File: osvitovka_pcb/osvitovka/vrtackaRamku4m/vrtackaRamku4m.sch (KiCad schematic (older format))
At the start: 17 parts, among them J1 Screw_Terminal_01x01, J2 Screw_Terminal_01x01, J3 M+, J4 M-, K1 RSM822, Q1 BC817, U1 LM78M05_TO220

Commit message: Nový PCB.
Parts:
- added D1, D2: D, Diode_SMD:D_1206_3216Metric, symbol Device:D
- added H1, H2: MountingHole, MountingHole:MountingHole_3.2mm_M3_ISO14580, symbol Mechanical:MountingHole
- R1, R2, R3, R4: footprint Resistor_SMD:R_1206_3216Metric_Pad1.42x1.75mm_HandSolder -> Resistor_SMD:R_0805_2012Metric
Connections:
- net +12V: now also D1.1 (K)
- net +5V: now also R4.2
- net GND: now also D2.2 (A)
- net at J3.1 (Pin_1), K1.14, K1.24: now also D2.1 (K)
- net at K1.A1, Q1.3 (C): now also D1.2 (A)
- net Led_green: no longer names the net of A1.13 (D10)
- net Led_green: no longer R4.2
- no-connect marks 25 -> 26
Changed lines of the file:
@@
 F 0 "R1" V 5143 2600 50  0000 C CNN
 F 1 "4k7" V 5234 2600 50  0000 C CNN
-F 2 "Resistor_SMD:R_1206_3216Metric_Pad1.42x1.75mm_HandSolder" V 5280 2600 50  0001 C CNN
+F 2 "Resistor_SMD:R_0805_2012Metric" V 5280 2600 50  0001 C CNN
 F 3 "~" H 5350 2600 50  0001 C CNN
 	1    5350 2600
@@
 F 0 "R3" V 1543 4600 50  0000 C CNN
 F 1 "470" V 1634 4600 50  0000 C CNN
-F 2 "Resistor_SMD:R_1206_3216Metric_Pad1.42x1.75mm_HandSolder" V 1680 4600 50  0001 C CNN
+F 2 "Resistor_SMD:R_0805_2012Metric" V 1680 4600 50  0001 C CNN
 F 3 "~" H 1750 4600 50  0001 C CNN
 	1    1750 4600
@@
 Text GLabel 1400 4600 0    50   Input ~ 0
 Led_yellow
-Text GLabel 1400 5050 0    50   Input ~ 0
-Led_green
 $Comp
 L Device:R R4
@@
 F 0 "R4" V 1543 5050 50  0000 C CNN
 F 1 "470" V 1634 5050 50  0000 C CNN
-F 2 "Resistor_SMD:R_1206_3216Metric_Pad1.42x1.75mm_HandSolder" V 1680 5050 50  0001 C CNN
+F 2 "Resistor_SMD:R_0805_2012Metric" V 1680 5050 50  0001 C CNN
 F 3 "~" H 1750 5050 50  0001 C CNN
 	1    1750 5050
@@
 Text GLabel 8500 3350 0    50   Input ~ 0
 Led_yellow
-Text GLabel 8500 3450 0    50   Input ~ 0
-Led_green
 Wire Wire Line
 	1250 3600 1400 3600
@@
 NoConn ~ 10050 2550
 NoConn ~ 10050 2450
-Wire Wire Line
-	8500 3450 9050 3450
 NoConn ~ 9050 2450
 NoConn ~ 9050 2650
@@
 	7000 2850 7000 3050
 Wire Wire Line
-	6100 2200 6100 2400
+	6100 2200 6100 2300
 $Comp
 L power:+12V #PWR03
@@
 $EndComp
 Wire Wire Line
-	6100 1450 6100 1600
+	6100 1450 6100 1550
 $Comp
 L power:GND #PWR011
@@
 F 0 "R2" V 5443 2800 50  0000 C CNN
 F 1 "10k" V 5534 2800 50  0000 C CNN
-F 2 "Resistor_SMD:R_1206_3216Metric_Pad1.42x1.75mm_HandSolder" V 5580 2800 50  0001 C CNN
+F 2 "Resistor_SMD:R_0805_2012Metric" V 5580 2800 50  0001 C CNN
 F 3 "~" H 5650 2800 50  0001 C CNN
 	1    5650 2800
@@
 NoConn ~ 6400 2200
 NoConn ~ 6800 2200
+$Comp
+L Mechanical:MountingHole H1
+U 1 1 5FD664D9
+P 1000 5500
+F 0 "H1" H 1100 5546 50  0000 L CNN
+F 1 "MountingHole" H 1100 5455 50  0000 L CNN
+F 2 "MountingHole:MountingHole_3.2mm_M3_ISO14580" H 1000 5500 50  0001 C CNN
+F 3 "~" H 1000 5500 50  0001 C CNN
+	1    1000 5500
+	1    0    0    -1
+$EndComp
+$Comp
+L Mechanical:MountingHole H2
+U 1 1 5FD66F45
+P 1000 5700
+F 0 "H2" H 1100 5746 50  0000 L CNN
+F 1 "MountingHole" H 1100 5655 50  0000 L CNN
+F 2 "MountingHole:MountingHole_3.2mm_M3_ISO14580" H 1000 5700 50  0001 C CNN
+F 3 "~" H 1000 5700 50  0001 C CNN
+	1    1000 5700
+	1    0    0    -1
+$EndComp
+$Comp
+L Device:D D2
+U 1 1 5FD94B8B
+P 7000 2650
+F 0 "D2" V 6954 2729 50  0000 L CNN
+F 1 "D" V 7045 2729 50  0000 L CNN
+F 2 "Diode_SMD:D_1206_3216Metric" H 7000 2650 50  0001 C CNN
+F 3 "~" H 7000 2650 50  0001 C CNN
+	1    7000 2650
+	0    1    1    0
+$EndComp
+$Comp
+L Device:D D1
+U 1 1 5FD95C5D
+P 5700 1900
+F 0 "D1" H 5700 2116 50  0000 C CNN
+F 1 "D" H 5700 2025 50  0000 C CNN
+F 2 "Diode_SMD:D_1206_3216Metric" H 5700 1900 50  0001 C CNN
+F 3 "~" H 5700 1900 50  0001 C CNN
+	1    5700 1900
+	0    1    1    0
+$EndComp
+Wire Wire Line
+	5700 1750 5700 1550
+Wire Wire Line
+	5700 1550 6100 1550
+Connection ~ 6100 1550
+Wire Wire Line
+	6100 1550 6100 1600
+Wire Wire Line
+	5700 2050 5700 2300
+Wire Wire Line
+	5700 2300 6100 2300
+Connection ~ 6100 2300
+Wire Wire Line
+	6100 2300 6100 2400
+Wire Wire Line
+	7000 2800 7000 2850
+Connection ~ 7000 2850
+Wire Wire Line
+	7000 2500 7000 2450
+$Comp
+L power:+5V #PWR?
+U 1 1 5FDA6872
+P 1400 5050
+F 0 "#PWR?" H 1400 4900 50  0001 C CNN
+F 1 "+5V" V 1415 5178 50  0000 L CNN
+F 2 "" H 1400 5050 50  0001 C CNN
+F 3 "" H 1400 5050 50  0001 C CNN
+	1    1400 5050
+	0    -1   -1   0
+$EndComp
+NoConn ~ 9050 3450
 $EndSCHEMATC

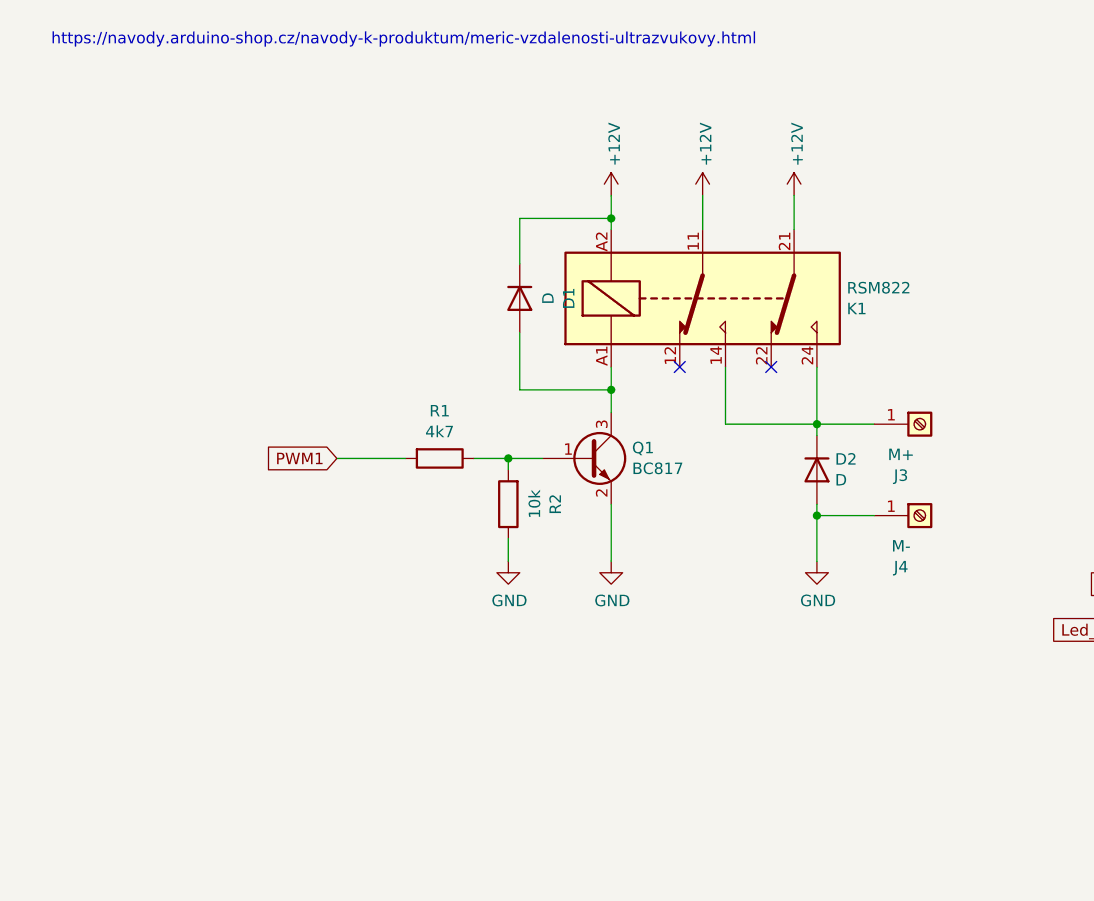
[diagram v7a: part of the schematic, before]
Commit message: Měl jsem špatný pouzdro na relátku. Opraveno.
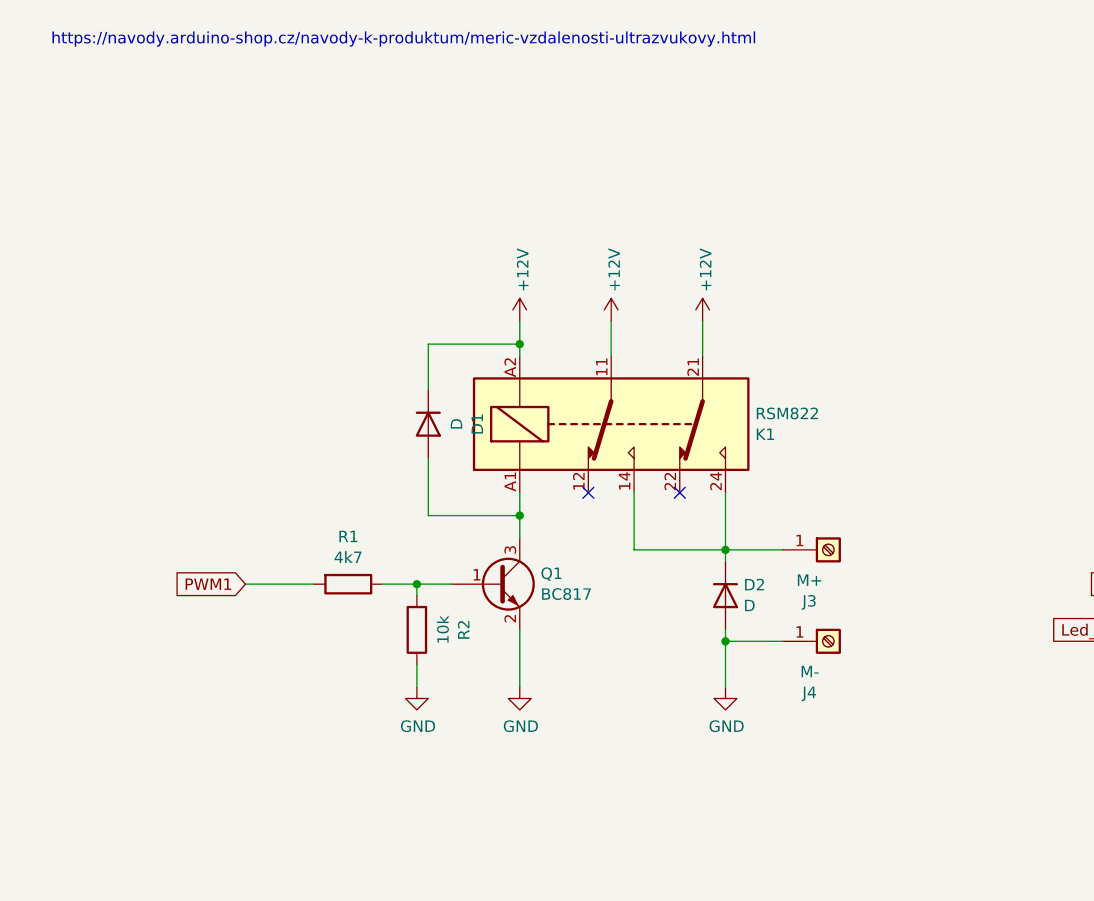
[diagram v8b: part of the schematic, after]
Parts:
- K1: footprint Relay_THT:Relay_DPDT_Finder_40.52 -> Relay_THT:Relay_DPDT_Finder_30.22
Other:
- moved on the sheet: D1, D2, J3, J4, K1, Q1, R1, R2
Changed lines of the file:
@@
 L power:GND #PWR010
 U 1 1 5FCC4DA2
-P 5650 3050
-F 0 "#PWR010" H 5650 2800 50  0001 C CNN
-F 1 "GND" H 5655 2877 50  0000 C CNN
-F 2 "" H 5650 3050 50  0001 C CNN
-F 3 "" H 5650 3050 50  0001 C CNN
-	1    5650 3050
+P 5250 3600
+F 0 "#PWR010" H 5250 3350 50  0001 C CNN
+F 1 "GND" H 5255 3427 50  0000 C CNN
+F 2 "" H 5250 3600 50  0001 C CNN
+F 3 "" H 5250 3600 50  0001 C CNN
+	1    5250 3600
 	1    0    0    -1
 $EndComp
@@
 L Device:R R1
 U 1 1 5FCC5E82
-P 5350 2600
-F 0 "R1" V 5143 2600 50  0000 C CNN
-F 1 "4k7" V 5234 2600 50  0000 C CNN
-F 2 "Resistor_SMD:R_0805_2012Metric" V 5280 2600 50  0001 C CNN
-F 3 "~" H 5350 2600 50  0001 C CNN
-	1    5350 2600
-	0    1    1    0
-$EndComp
-Text GLabel 4900 2600 0    50   Input ~ 0
+P 4950 3150
+F 0 "R1" V 4743 3150 50  0000 C CNN
+F 1 "4k7" V 4834 3150 50  0000 C CNN
+F 2 "Resistor_SMD:R_0805_2012Metric" V 4880 3150 50  0001 C CNN
+F 3 "~" H 4950 3150 50  0001 C CNN
+	1    4950 3150
+	0    1    1    0
+$EndComp
+Text GLabel 4500 3150 0    50   Input ~ 0
 PWM1
 Wire Wire Line
-	4900 2600 5200 2600
+	4500 3150 4800 3150
 Text GLabel 8500 3150 0    50   Input ~ 0
 PWM1
@@
 L Connector:Screw_Terminal_01x01 J3
 U 1 1 5FD0CD16
-P 7450 2450
-F 0 "J3" H 7368 2225 50  0000 C CNN
-F 1 "M+" H 7368 2316 50  0000 C CNN
-F 2 "TestPoint:TestPoint_Loop_D3.80mm_Drill2.5mm" H 7450 2450 50  0001 C CNN
-F 3 "~" H 7450 2450 50  0001 C CNN
-	1    7450 2450
+P 7050 3000
+F 0 "J3" H 6968 2775 50  0000 C CNN
+F 1 "M+" H 6968 2866 50  0000 C CNN
+F 2 "TestPoint:TestPoint_Loop_D3.80mm_Drill2.5mm" H 7050 3000 50  0001 C CNN
+F 3 "~" H 7050 3000 50  0001 C CNN
+	1    7050 3000
 	1    0    0    -1
 $EndComp
@@
 L Connector:Screw_Terminal_01x01 J4
 U 1 1 5FD0DE67
-P 7450 2850
-F 0 "J4" H 7368 2625 50  0000 C CNN
-F 1 "M-" H 7368 2716 50  0000 C CNN
-F 2 "TestPoint:TestPoint_Loop_D3.80mm_Drill2.5mm" H 7450 2850 50  0001 C CNN
-F 3 "~" H 7450 2850 50  0001 C CNN
-	1    7450 2850
+P 7050 3400
+F 0 "J4" H 6968 3175 50  0000 C CNN
+F 1 "M-" H 6968 3266 50  0000 C CNN
+F 2 "TestPoint:TestPoint_Loop_D3.80mm_Drill2.5mm" H 7050 3400 50  0001 C CNN
+F 3 "~" H 7050 3400 50  0001 C CNN
+	1    7050 3400
 	1    0    0    -1
 $EndComp
@@
 L Transistor_BJT:BC817 Q1
 U 1 1 5FD6B85F
-P 6000 2600
-F 0 "Q1" H 6191 2646 50  0000 L CNN
-F 1 "BC817" H 6191 2555 50  0000 L CNN
-F 2 "Package_TO_SOT_SMD:SOT-23" H 6200 2525 50  0001 L CIN
-F 3 "http://www.fairchildsemi.com/ds/BC/BC817.pdf" H 6000 2600 50  0001 L CNN
-	1    6000 2600
+P 5600 3150
+F 0 "Q1" H 5791 3196 50  0000 L CNN
+F 1 "BC817" H 5791 3105 50  0000 L CNN
+F 2 "Package_TO_SOT_SMD:SOT-23" H 5800 3075 50  0001 L CIN
+F 3 "http://www.fairchildsemi.com/ds/BC/BC817.pdf" H 5600 3150 50  0001 L CNN
+	1    5600 3150
 	1    0    0    -1
 $EndComp
@@
 L Relay:RSM822 K1
 U 1 1 5FD72A40
-P 6500 1900
-F 0 "K1" H 7130 1946 50  0000 L CNN
-F 1 "RSM822" H 7130 1855 50  0000 L CNN
-F 2 "Relay_THT:Relay_DPDT_Finder_40.52" H 7850 1870 50  0001 C CNN
-F 3 "http://www.relpol.pl/en/content/download/14975/202519/file/e_RSM822.pdf" H 6500 1900 50  0001 C CNN
-	1    6500 1900
+P 6100 2450
+F 0 "K1" H 6730 2496 50  0000 L CNN
+F 1 "RSM822" H 6730 2405 50  0000 L CNN
+F 2 "Relay_THT:Relay_DPDT_Finder_30.22" H 7450 2420 50  0001 C CNN
+F 3 "http://www.relpol.pl/en/content/download/14975/202519/file/e_RSM822.pdf" H 6100 2450 50  0001 C CNN
+	1    6100 2450
 	1    0    0    1
 $EndComp
@@
 L power:+12V #PWR04
 U 1 1 5FD831EA
-P 6500 1450
-F 0 "#PWR04" H 6500 1300 50  0001 C CNN
-F 1 "+12V" V 6515 1578 50  0000 L CNN
-F 2 "" H 6500 1450 50  0001 C CNN
-F 3 "" H 6500 1450 50  0001 C CNN
-	1    6500 1450
+P 6100 2000
+F 0 "#PWR04" H 6100 1850 50  0001 C CNN
+F 1 "+12V" V 6115 2128 50  0000 L CNN
+F 2 "" H 6100 2000 50  0001 C CNN
+F 3 "" H 6100 2000 50  0001 C CNN
+	1    6100 2000
 	1    0    0    -1
 $EndComp
@@
 L power:+12V #PWR05
 U 1 1 5FD83A62
-P 6900 1450
-F 0 "#PWR05" H 6900 1300 50  0001 C CNN
-F 1 "+12V" V 6915 1578 50  0000 L CNN
-F 2 "" H 6900 1450 50  0001 C CNN
-F 3 "" H 6900 1450 50  0001 C CNN
-	1    6900 1450
-	1    0    0    -1
-$EndComp
-Wire Wire Line
-	6500 1450 6500 1600
-Wire Wire Line
-	6900 1450 6900 1600
-Wire Wire Line
-	7250 2450 7000 2450
-Wire Wire Line
-	6600 2450 6600 2200
-Wire Wire Line
-	7000 2200 7000 2450
-Connection ~ 7000 2450
-Wire Wire Line
-	7000 2450 6600 2450
+P 6500 2000
+F 0 "#PWR05" H 6500 1850 50  0001 C CNN
+F 1 "+12V" V 6515 2128 50  0000 L CNN
+F 2 "" H 6500 2000 50  0001 C CNN
+F 3 "" H 6500 2000 50  0001 C CNN
+	1    6500 2000
+	1    0    0    -1
+$EndComp
+Wire Wire Line
+	6100 2000 6100 2150
+Wire Wire Line
+	6500 2000 6500 2150
+Wire Wire Line
+	6850 3000 6600 3000
+Wire Wire Line
+	6200 3000 6200 2750
+Wire Wire Line
+	6600 2750 6600 3000
+Connection ~ 6600 3000
+Wire Wire Line
+	6600 3000 6200 3000
 $Comp
 L power:GND #PWR012
 U 1 1 5FD86ED6
-P 7000 3050
-F 0 "#PWR012" H 7000 2800 50  0001 C CNN
-F 1 "GND" H 7005 2877 50  0000 C CNN
-F 2 "" H 7000 3050 50  0001 C CNN
-F 3 "" H 7000 3050 50  0001 C CNN
-	1    7000 3050
-	1    0    0    -1
-$EndComp
-Wire Wire Line
-	7250 2850 7000 2850
-Wire Wire Line
-	7000 2850 7000 3050
-Wire Wire Line
-	6100 2200 6100 2300
+P 6600 3600
+F 0 "#PWR012" H 6600 3350 50  0001 C CNN
+F 1 "GND" H 6605 3427 50  0000 C CNN
+F 2 "" H 6600 3600 50  0001 C CNN
+F 3 "" H 6600 3600 50  0001 C CNN
+	1    6600 3600
+	1    0    0    -1
+$EndComp
+Wire Wire Line
+	6850 3400 6600 3400
+Wire Wire Line
+	6600 3400 6600 3600
+Wire Wire Line
+	5700 2750 5700 2850
 $Comp
 L power:+12V #PWR03
 U 1 1 5FD8968E
-P 6100 1450
-F 0 "#PWR03" H 6100 1300 50  0001 C CNN
-F 1 "+12V" V 6115 1578 50  0000 L CNN
-F 2 "" H 6100 1450 50  0001 C CNN
-F 3 "" H 6100 1450 50  0001 C CNN
-	1    6100 1450
-	1    0    0    -1
-$EndComp
-Wire Wire Line
-	6100 1450 6100 1550
+P 5700 2000
+F 0 "#PWR03" H 5700 1850 50  0001 C CNN
+F 1 "+12V" V 5715 2128 50  0000 L CNN
+F 2 "" H 5700 2000 50  0001 C CNN
+F 3 "" H 5700 2000 50  0001 C CNN
+	1    5700 2000
+	1    0    0    -1
+$EndComp
+Wire Wire Line
+	5700 2000 5700 2100
 $Comp
 L power:GND #PWR011
 U 1 1 5FD8A380
-P 6100 3050
-F 0 "#PWR011" H 6100 2800 50  0001 C CNN
-F 1 "GND" H 6105 2877 50  0000 C CNN
-F 2 "" H 6100 3050 50  0001 C CNN
-F 3 "" H 6100 3050 50  0001 C CNN
-	1    6100 3050
-	1    0    0    -1
-$EndComp
-Wire Wire Line
-	6100 2800 6100 3050
+P 5700 3600
+F 0 "#PWR011" H 5700 3350 50  0001 C CNN
+F 1 "GND" H 5705 3427 50  0000 C CNN
+F 2 "" H 5700 3600 50  0001 C CNN
+F 3 "" H 5700 3600 50  0001 C CNN
+	1    5700 3600
+	1    0    0    -1
+$EndComp
+Wire Wire Line
+	5700 3350 5700 3600
 $Comp
 L Device:R R2
 U 1 1 5FD8CC29
-P 5650 2800
-F 0 "R2" V 5443 2800 50  0000 C CNN
-F 1 "10k" V 5534 2800 50  0000 C CNN
-F 2 "Resistor_SMD:R_0805_2012Metric" V 5580 2800 50  0001 C CNN
-F 3 "~" H 5650 2800 50  0001 C CNN
-	1    5650 2800
+P 5250 3350
+F 0 "R2" V 5043 3350 50  0000 C CNN
+F 1 "10k" V 5134 3350 50  0000 C CNN
+F 2 "Resistor_SMD:R_0805_2012Metric" V 5180 3350 50  0001 C CNN
+F 3 "~" H 5250 3350 50  0001 C CNN
+	1    5250 3350
 	-1   0    0    1
 $EndComp
 Wire Wire Line
-	5500 2600 5650 2600
-Wire Wire Line
-	5650 2650 5650 2600
-Connection ~ 5650 2600
-Wire Wire Line
-	5650 2600 5800 2600
-Wire Wire Line
-	5650 2950 5650 3050
-NoConn ~ 6400 2200
-NoConn ~ 6800 2200
+	5100 3150 5250 3150
+Wire Wire Line
+	5250 3200 5250 3150
+Connection ~ 5250 3150
+Wire Wire Line
+	5250 3150 5400 3150
+Wire Wire Line
+	5250 3500 5250 3600
+NoConn ~ 6000 2750
+NoConn ~ 6400 2750
 $Comp
 L Mechanical:MountingHole H1
@@
 L Device:D D2
 U 1 1 5FD94B8B
-P 7000 2650
-F 0 "D2" V 6954 2729 50  0000 L CNN
-F 1 "D" V 7045 2729 50  0000 L CNN
-F 2 "Diode_SMD:D_1206_3216Metric" H 7000 2650 50  0001 C CNN
-F 3 "~" H 7000 2650 50  0001 C CNN
-	1    7000 2650
+P 6600 3200
+F 0 "D2" V 6554 3279 50  0000 L CNN
+F 1 "D" V 6645 3279 50  0000 L CNN
+F 2 "Diode_SMD:D_1206_3216Metric" H 6600 3200 50  0001 C CNN
+F 3 "~" H 6600 3200 50  0001 C CNN
+	1    6600 3200
 	0    1    1    0
 $EndComp
@@
 L Device:D D1
 U 1 1 5FD95C5D
-P 5700 1900
-F 0 "D1" H 5700 2116 50  0000 C CNN
-F 1 "D" H 5700 2025 50  0000 C CNN
-F 2 "Diode_SMD:D_1206_3216Metric" H 5700 1900 50  0001 C CNN
-F 3 "~" H 5700 1900 50  0001 C CNN
-	1    5700 1900
-	0    1    1    0
-$EndComp
-Wire Wire Line
-	5700 1750 5700 1550
-Wire Wire Line
-	5700 1550 6100 1550
-Connection ~ 6100 1550
-Wire Wire Line
-	6100 1550 6100 1600
-Wire Wire Line
-	5700 2050 5700 2300
-Wire Wire Line
-	5700 2300 6100 2300
-Connection ~ 6100 2300
-Wire Wire Line
-	6100 2300 6100 2400
-Wire Wire Line
-	7000 2800 7000 2850
-Connection ~ 7000 2850
-Wire Wire Line
-	7000 2500 7000 2450
-$Comp
-L power:+5V #PWR?
+P 5300 2450
+F 0 "D1" H 5300 2666 50  0000 C CNN
+F 1 "D" H 5300 2575 50  0000 C CNN
+F 2 "Diode_SMD:D_1206_3216Metric" H 5300 2450 50  0001 C CNN
+F 3 "~" H 5300 2450 50  0001 C CNN
+	1    5300 2450
+	0    1    1    0
+$EndComp
+Wire Wire Line
+	5300 2300 5300 2100
+Wire Wire Line
+	5300 2100 5700 2100
+Connection ~ 5700 2100
+Wire Wire Line
+	5700 2100 5700 2150
+Wire Wire Line
+	5300 2600 5300 2850
+Wire Wire Line
+	5300 2850 5700 2850
+Connection ~ 5700 2850
+Wire Wire Line
+	5700 2850 5700 2950
+Wire Wire Line
+	6600 3350 6600 3400
+Connection ~ 6600 3400
+Wire Wire Line
+	6600 3050 6600 3000
+$Comp
+L power:+5V #PWR0101
 U 1 1 5FDA6872
 P 1400 5050
-F 0 "#PWR?" H 1400 4900 50  0001 C CNN
+F 0 "#PWR0101" H 1400 4900 50  0001 C CNN
 F 1 "+5V" V 1415 5178 50  0000 L CNN
 F 2 "" H 1400 5050 50  0001 C CNN
